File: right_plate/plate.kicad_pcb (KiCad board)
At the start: 2 copper layers, 216.6 x 96 mm, 36 parts

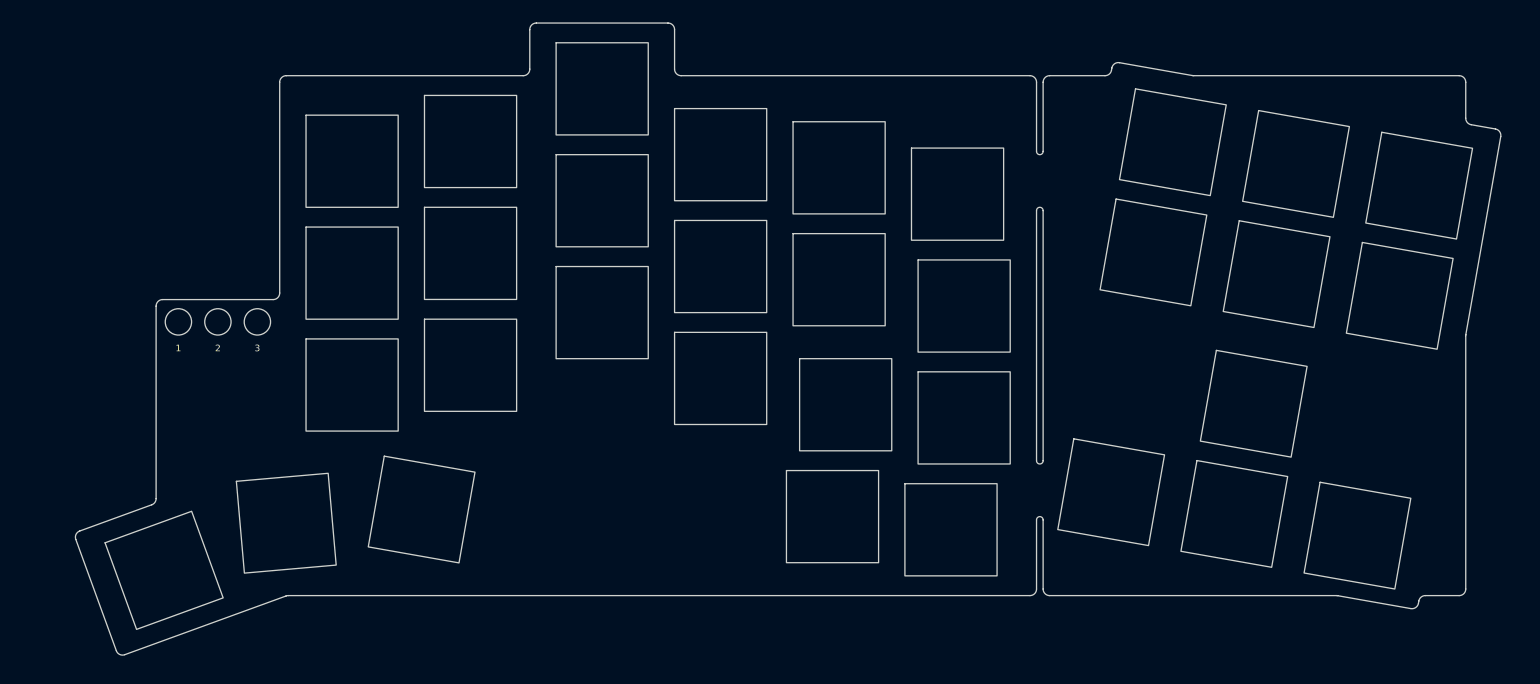
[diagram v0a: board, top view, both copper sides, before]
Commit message: add left plate; update hole footprints; update STEP files
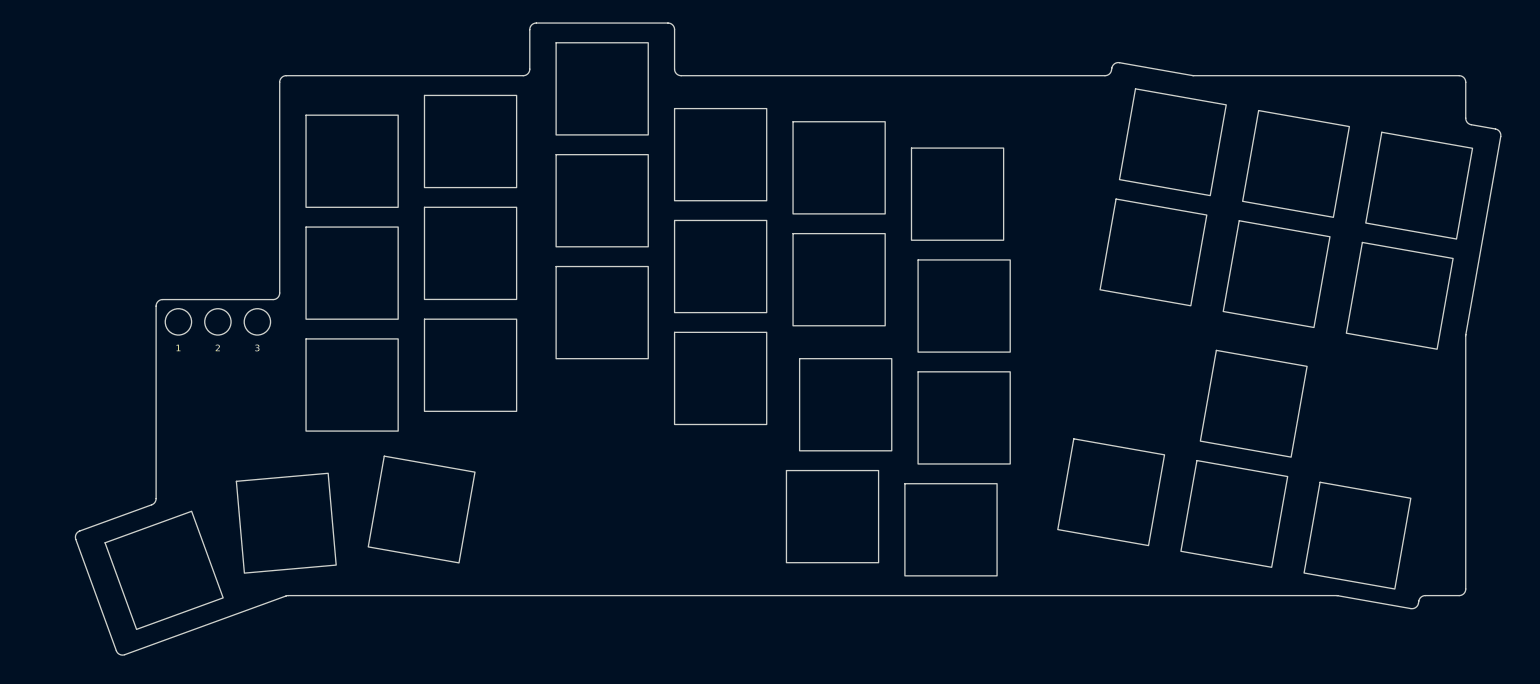
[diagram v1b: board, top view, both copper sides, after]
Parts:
- SW43, SW45, SW46, SW47, SW48, SW49: footprint Library:Switch -> Plate:Switch
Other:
- outline, holes or cut-outs redrawn

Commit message: change snap off thickness to 1.6mm for fab house
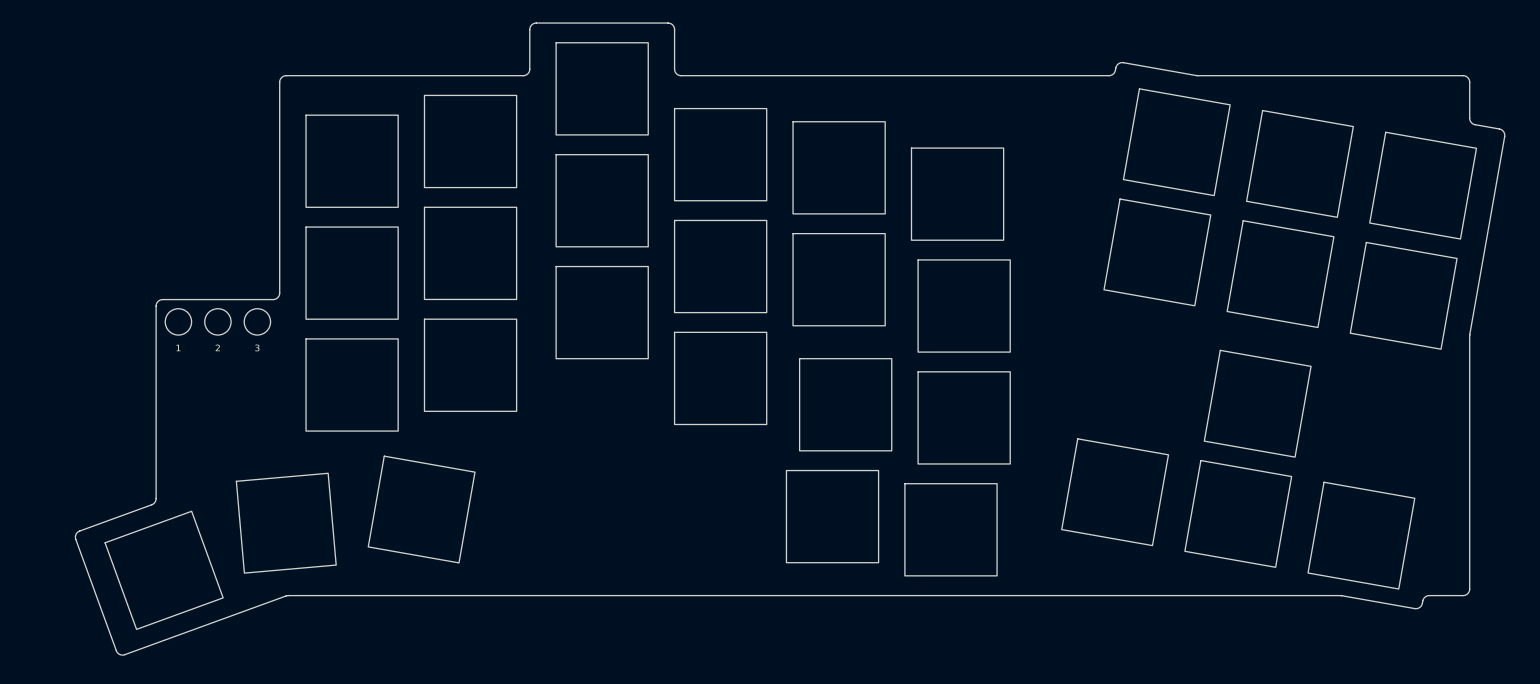
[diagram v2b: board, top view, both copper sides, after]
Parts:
- moved SW19 0.60 mm to (244.2, 66.2)
- moved SW17 0.60 mm to (206.8, 59.6)
- moved SW18 0.60 mm to (225.5, 62.9)
- moved SW27 0.60 mm to (203.9, 76.4)
- moved SW28 0.60 mm to (222.6, 79.7)
- moved SW29 0.60 mm to (241.3, 83.0)
- moved SW38 0.60 mm to (219.1, 99.3)
- moved SW47 0.60 mm to (197.4, 112.8)
- moved SW48 0.60 mm to (216.2, 116.1)
- moved SW49 0.60 mm to (234.9, 119.4)
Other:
- board size 216.6 x 96 mm -> 217.2 x 96 mm

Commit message: adjust LED footprint to T1 standard
update plates and traces
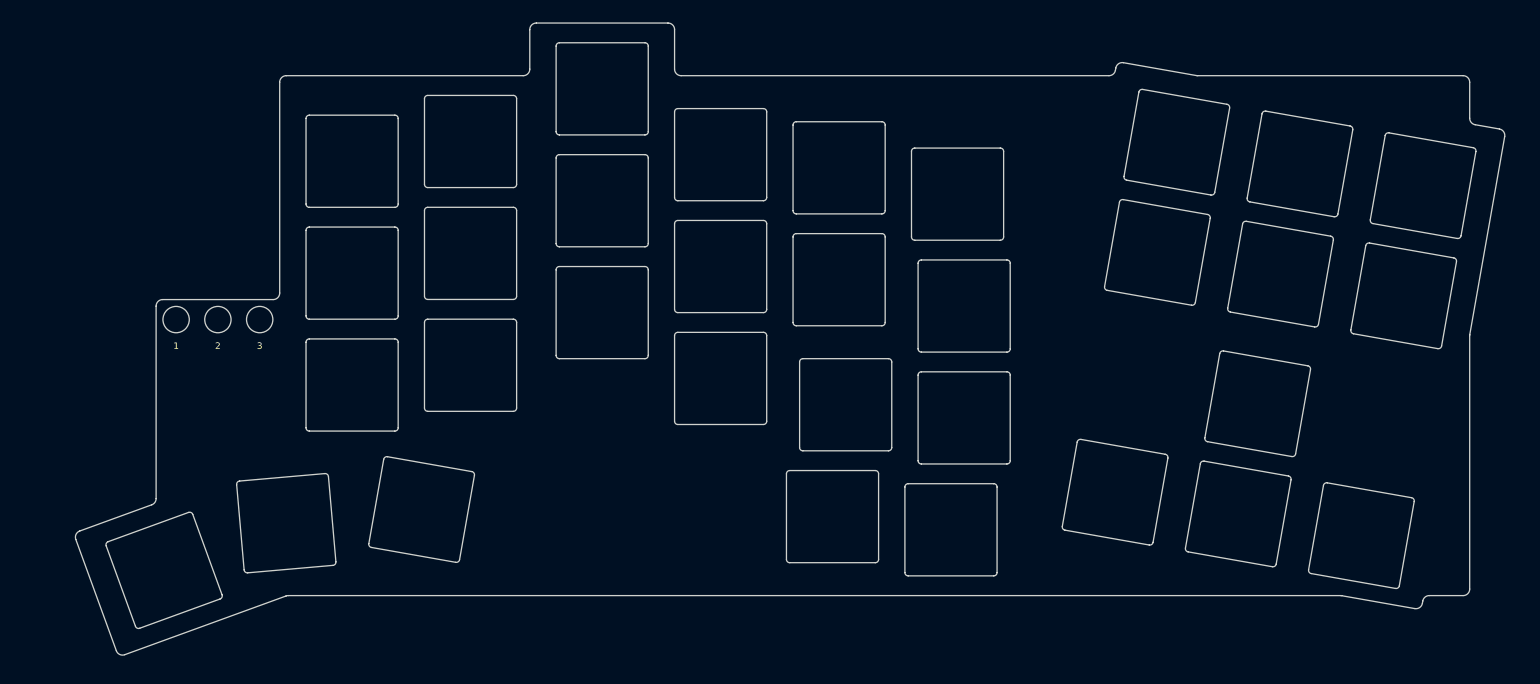
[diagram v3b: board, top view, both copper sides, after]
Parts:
- moved D1 0.49 mm to (54.8, 86.6)
- moved D3 0.49 mm to (67.5, 86.6)
- moved D2 0.35 mm to (61.1, 86.6)

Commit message: add copper fill to plates and correct plate silkscreen
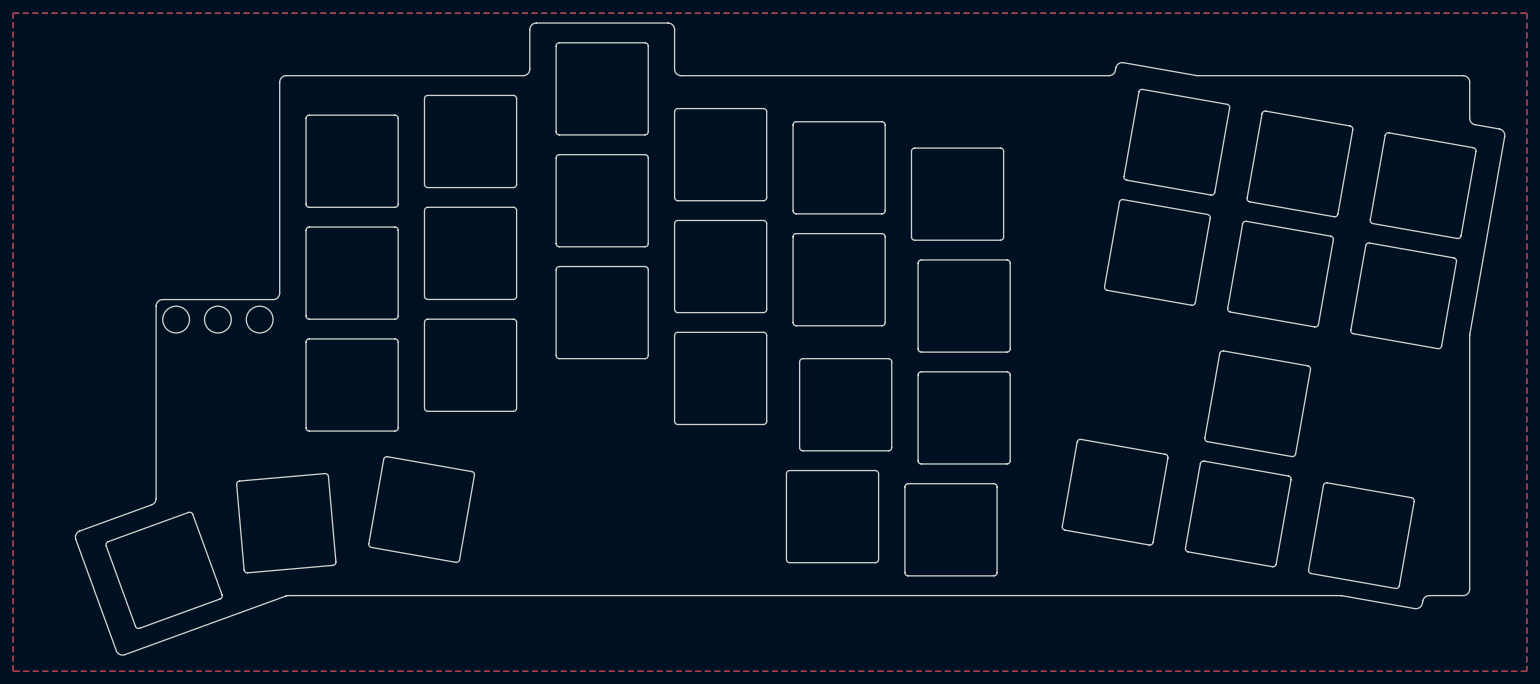
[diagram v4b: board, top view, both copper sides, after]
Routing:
- added copper zone on B.Cu, net (none)
- added copper zone on F.Cu, net (none)
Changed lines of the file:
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@@
     (property "Sheetfile" "plate.kicad_sch")
     (property "Sheetname" "")
-    (fp_text reference "D2" (at 0 0 unlocked) (layer "Dwgs.User") hide
-        (effects (font (size 1 1) (thickness 0.1)))
-    )
-    (fp_text value "2" (at 0 2 unlocked) (layer "F.Fab") hide
-        (effects (font (size 1 1) (thickness 0.1)))
-    )
-    (fp_text user "${VALUE}" (at 0 4 unlocked) (layer "F.SilkS")
-        (effects (font (size 1 1) (thickness 0.15)))
-    )
-    (fp_circle (center 0 0) (end 2 0)
+    (fp_text reference "D2" (at 0 -1 unlocked) (layer "Dwgs.User") hide
+        (effects (font (size 1 1) (thickness 0.1)))
+    )
+    (fp_text value "2" (at 0 1 unlocked) (layer "F.Fab") hide
+        (effects (font (size 1 1) (thickness 0.1)))
+    )
+    (fp_text user "${VALUE}" (at 0 3.81 unlocked) (layer "B.SilkS")
+        (effects (font (size 1.5 1.5) (thickness 0.15)) (justify mirror))
+    )
+    (fp_text user "${VALUE}" (at 0 3.81 unlocked) (layer "F.SilkS")
+        (effects (font (size 1.5 1.5) (thickness 0.15)))
+    )
+    (fp_circle (center 0 0) (end 2.032 0)
       (stroke (width 0.05) (type default)) (fill none) (layer "Edge.Cuts"))
   )
@@
     (property "Sheetfile" "plate.kicad_sch")
     (property "Sheetname" "")
-    (fp_text reference "D1" (at 0 0 unlocked) (layer "Dwgs.User") hide
-        (effects (font (size 1 1) (thickness 0.1)))
-    )
-    (fp_text value "1" (at 0 2 unlocked) (layer "F.Fab") hide
-        (effects (font (size 1 1) (thickness 0.1)))
-    )
-    (fp_text user "${VALUE}" (at 0 4 unlocked) (layer "F.SilkS")
-        (effects (font (size 1 1) (thickness 0.15)))
-    )
-    (fp_circle (center 0 0) (end 2 0)
+    (fp_text reference "D1" (at 0 -1 unlocked) (layer "Dwgs.User") hide
+        (effects (font (size 1 1) (thickness 0.1)))
+    )
+    (fp_text value "1" (at 0 1 unlocked) (layer "F.Fab") hide
+        (effects (font (size 1 1) (thickness 0.1)))
+    )
+    (fp_text user "${VALUE}" (at 0 3.81 unlocked) (layer "B.SilkS")
+        (effects (font (size 1.5 1.5) (thickness 0.15)) (justify mirror))
+    )
+    (fp_text user "${VALUE}" (at 0 3.81 unlocked) (layer "F.SilkS")
+        (effects (font (size 1.5 1.5) (thickness 0.15)))
+    )
+    (fp_circle (center 0 0) (end 2.032 0)
       (stroke (width 0.05) (type default)) (fill none) (layer "Edge.Cuts"))
   )
@@
     (property "Sheetfile" "plate.kicad_sch")
     (property "Sheetname" "")
-    (fp_text reference "D3" (at 0 0 unlocked) (layer "Dwgs.User") hide
-        (effects (font (size 1 1) (thickness 0.1)))
-    )
-    (fp_text value "3" (at 0 2 unlocked) (layer "F.Fab") hide
-        (effects (font (size 1 1) (thickness 0.1)))
-    )
-    (fp_text user "${VALUE}" (at 0 4 unlocked) (layer "F.SilkS")
-        (effects (font (size 1 1) (thickness 0.15)))
-    )
-    (fp_circle (center 0 0) (end 2 0)
+    (fp_text reference "D3" (at 0 -1 unlocked) (layer "Dwgs.User") hide
+        (effects (font (size 1 1) (thickness 0.1)))
+    )
+    (fp_text value "3" (at 0 1 unlocked) (layer "F.Fab") hide
+        (effects (font (size 1 1) (thickness 0.1)))
+    )
+    (fp_text user "${VALUE}" (at 0 3.81 unlocked) (layer "B.SilkS")
+        (effects (font (size 1.5 1.5) (thickness 0.15)) (justify mirror))
+    )
+    (fp_text user "${VALUE}" (at 0 3.81 unlocked) (layer "F.SilkS")
+        (effects (font (size 1.5 1.5) (thickness 0.15)))
+    )
+    (fp_circle (center 0 0) (end 2.032 0)
       (stroke (width 0.05) (type default)) (fill none) (layer "Edge.Cuts"))
   )
@@
   (gr_line (start 69.5 83.52) (end 52.72 83.52)
     (stroke (width 0.1) (type solid)) (layer "Edge.Cuts"))
+  (zone (net 0) (net_name "") (layers "F&B.Cu") (hatch edge 0.5)
+    (connect_pads (clearance 0.5))
+    (min_thickness 0.25) (filled_areas_thickness no)
+    (fill yes (thermal_gap 0.5) (thermal_bridge_width 0.5) (island_removal_mode 1) (island_area_min 10))
+    (polygon
+      (pts
+        (xy 260 40)
+        (xy 260 140)
+        (xy 30 140)
+        (xy 30 40)
+      )
+    )
+  )
 )
